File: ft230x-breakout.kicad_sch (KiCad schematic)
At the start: 19 parts, among them J101 USB_B_Micro, J103 Conn_01x05_Pin, J104 Conn_01x05_Pin, U101 FT230XS

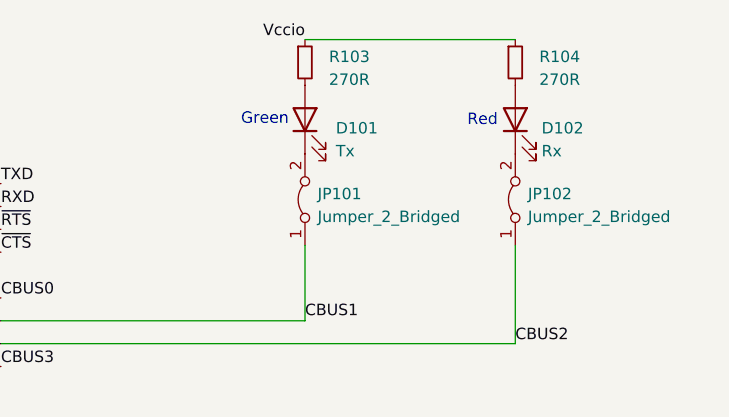
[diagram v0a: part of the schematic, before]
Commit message: Correct a silkscreen problem on rev 1.0 of the board: Tx and Rx LED labels were swapped.  Bump rev to 1.1.
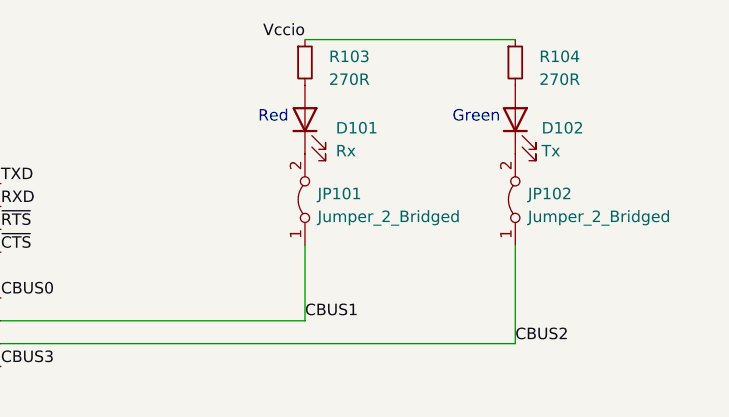
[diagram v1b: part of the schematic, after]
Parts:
- D101: value Tx -> Rx
- D102: value Rx -> Tx
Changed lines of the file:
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@@
   (title_block
     (title "FT230X Breakout")
-    (date "2024-07-03")
-    (rev "1.0")
+    (date "2024-07-05")
+    (rev "1.1")
     (company "Copyright (c) 2024 Jason R. Thorpe.  See LICENSE.")
   )
@@
     (stroke (width 0) (type default))
   )
-  (text "Red" (at 224.155 72.009 0)
-    (effects (font (size 1.27 1.27)) (justify left bottom))
-  )
-  (text "Green" (at 199.009 71.882 0)
+  (text "Red" (at 200.914 71.628 0)
+    (effects (font (size 1.27 1.27)) (justify left bottom))
+  )
+  (text "Green" (at 222.504 71.628 0)
     (effects (font (size 1.27 1.27)) (justify left bottom))
   )
@@
       (effects (font (size 1.27 1.27)) (justify right))
     )
-    (property "Value" "Rx" (at 232.41 74.6125 90)
+    (property "Value" "Tx" (at 232.41 74.6125 90)
       (effects (font (size 1.27 1.27)) (justify right))
     )
@@
       (effects (font (size 1.27 1.27)) (justify right))
     )
-    (property "Value" "Tx" (at 209.55 74.6125 90)
-      (effects (font (size 1.27 1.27)) (justify right))
-    )
+    (property "Value" "Rx" (at 209.55 74.6125 90)
+      (effects (font (size 1.27 1.27)) (justify right))
+    )
